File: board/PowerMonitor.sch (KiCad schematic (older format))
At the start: 0 parts

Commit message: Issue #934 - GTP routing
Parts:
- added C173, C174: C, ~, symbol C
- added U17: MAX4377, symbol MAX4377
- added U18: MAX4378, symbol MAX4378
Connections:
- new net DDR0V9_RS+: U18.10 (RS3+)
- new net DDR0V9_RS-: U18.9 (RS3-)
- new net DDR1V8_RS+: U18.12 (RS4+)
- new net DDR1V8_RS-: U18.13 (RS4-)
- new net GND: C173.2, C174.2, U17.4 (GND), U18.11 (GND)
- new net PICADC10: U18.8 (OUT3)
- new net PICADC11: U18.14 (OUT4)
- new net PICADC6: U17.1 (OUT1)
- new net PICADC7: U17.7 (OUT2)
- new net PICADC8: U18.1 (OUT1)
- new net PICADC9: U18.7 (OUT2)
- new net VCC12V0_RS+: U17.3 (RS1+)
- new net VCC12V0_RS-: U17.2 (RS1-)
- new net VCC1V2_RS+: U18.5 (RS2+)
- new net VCC1V2_RS-: U18.6 (RS2-)
- new net VCC3V3_RS+: U18.3 (RS1+)
- new net VCC3V3_RS-: U18.2 (RS1-)
- new net VCC5V0: C173.1, C174.1, U17.8 (VCC), U18.4 (VCC)
- new net VCC5V0_RS+: U17.5 (RS2+)
- new net VCC5V0_RS-: U17.6 (RS2-)
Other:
- note added: "CURRENT MONITORING"
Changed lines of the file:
@@
 $Descr A4 11693 8268
 encoding utf-8
-Sheet 7 8
+Sheet 8 8
 Title ""
-Date "25 feb 2014"
+Date "27 feb 2014"
 Rev ""
 Comp ""
@@
 Comment4 ""
 $EndDescr
+$Comp
+L MAX4377 U17
+U 1 1 530F8241
+P 1650 1350
+F 0 "U17" H 1950 1000 60  0000 C CNN
+F 1 "MAX4377" H 1550 1650 60  0000 C CNN
+F 2 "" H 1650 1350 60  0000 C CNN
+F 3 "" H 1650 1350 60  0000 C CNN
+	1    1650 1350
+	1    0    0    -1
+$EndComp
+$Comp
+L MAX4378 U18
+U 1 1 530F8250
+P 4250 1450
+F 0 "U18" H 4500 1000 60  0000 C CNN
+F 1 "MAX4378" H 4150 1900 60  0000 C CNN
+F 2 "" H 6150 100 60  0000 C CNN
+F 3 "" H 6150 100 60  0000 C CNN
+	1    4250 1450
+	1    0    0    -1
+$EndComp
+Text GLabel 2500 1200 2    39   Input ~ 0
+VCC5V0
+Wire Wire Line
+	2500 1200 2300 1200
+Text Label 2300 1200 0    39   ~ 0
+VCC5V0
+Text Label 3650 1450 2    39   ~ 0
+VCC5V0
+Text GLabel 850  1500 0    39   Input ~ 0
+GND
+Wire Wire Line
+	1050 1500 850  1500
+Text Label 850  1500 0    39   ~ 0
+GND
+Text Label 1050 1200 2    39   ~ 0
+PICADC6
+Text Label 2300 1300 0    39   ~ 0
+PICADC7
+Text Label 3650 1150 2    39   ~ 0
+PICADC8
+Text Label 3650 1750 2    39   ~ 0
+PICADC9
+Text Label 4850 1750 0    39   ~ 0
+PICADC10
+Text Label 4850 1150 0    39   ~ 0
+PICADC11
+Text HLabel 1050 1400 0    39   Input ~ 0
+VCC12V0_RS+
+Text HLabel 1050 1300 0    39   Input ~ 0
+VCC12V0_RS-
+Text HLabel 2300 1500 2    39   Input ~ 0
+VCC5V0_RS+
+Text HLabel 2300 1400 2    39   Input ~ 0
+VCC5V0_RS-
+Text HLabel 3650 1350 0    39   Input ~ 0
+VCC3V3_RS+
+Text HLabel 3650 1250 0    39   Input ~ 0
+VCC3V3_RS-
+Text HLabel 3650 1550 0    39   Input ~ 0
+VCC1V2_RS+
+Text HLabel 3650 1650 0    39   Input ~ 0
+VCC1V2_RS-
+Text HLabel 4850 1350 2    39   Input ~ 0
+DDR1V8_RS+
+Text HLabel 4850 1250 2    39   Input ~ 0
+DDR1V8_RS-
+Text HLabel 4850 1650 2    39   Input ~ 0
+DDR0V9_RS-
+Text HLabel 4850 1550 2    39   Input ~ 0
+DDR0V9_RS+
+$Comp
+L C C173
+U 1 1 5311983F
+P 1850 2550
+F 0 "C173" H 1850 2650 40  0000 L CNN
+F 1 "C" H 1856 2465 40  0000 L CNN
+F 2 "~" H 1888 2400 30  0000 C CNN
+F 3 "~" H 1850 2550 60  0000 C CNN
+	1    1850 2550
+	1    0    0    -1
+$EndComp
+Text Label 1650 2300 0    39   ~ 0
+VCC5V0
+Wire Wire Line
+	1650 2300 2100 2300
+Wire Wire Line
+	1850 2300 1850 2350
+$Comp
+L C C174
+U 1 1 53119855
+P 2100 2550
+F 0 "C174" H 2100 2650 40  0000 L CNN
+F 1 "C" H 2106 2465 40  0000 L CNN
+F 2 "~" H 2138 2400 30  0000 C CNN
+F 3 "~" H 2100 2550 60  0000 C CNN
+	1    2100 2550
+	1    0    0    -1
+$EndComp
+Wire Wire Line
+	2100 2300 2100 2350
+Connection ~ 1850 2300
+Wire Wire Line
+	1650 2750 2100 2750
+Connection ~ 1850 2750
+Text Label 4850 1450 0    39   ~ 0
+GND
+Text Label 1650 2750 0    39   ~ 0
+GND
+Wire Bus Line
+	6200 500  6200 3000
+Wire Bus Line
+	6200 3000 500  3000
+Text Notes 5450 2950 0    39   ~ 0
+CURRENT MONITORING
+Text HLabel 1250 3750 0    39   Input ~ 0
+PICADC0
+Text HLabel 1250 3850 0    39   Input ~ 0
+PICADC1
+Text HLabel 1250 3950 0    39   Input ~ 0
+PICADC2
+Text HLabel 1250 4050 0    39   Input ~ 0
+PICADC3
+Text HLabel 1250 4150 0    39   Input ~ 0
+PICADC4
+Text HLabel 1250 4250 0    39   Input ~ 0
+PICADC5
 $EndSCHEMATC

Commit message: Issue #1022 - Power supply & pic
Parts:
- added U?: PIC18F85J50, ~, symbol PIC18F85J50
- added X?: CRYSTAL, ~, symbol CRYSTAL
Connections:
- net VCC5V0 renamed VCC3V3
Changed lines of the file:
@@
 EELAYER 27 0
 EELAYER END
-$Descr A4 11693 8268
+$Descr A3 16535 11693
 encoding utf-8
 Sheet 8 8
 Title ""
-Date "13 mar 2014"
+Date "14 mar 2014"
 Rev ""
 Comp ""
@@
 $EndComp
 Text GLabel 2500 1200 2    39   Input ~ 0
-VCC5V0
+VCC3V3
 Wire Wire Line
 	2500 1200 2300 1200
@@
 Text HLabel 1250 4250 0    39   Input ~ 0
 PICADC5
+$Comp
+L CRYSTAL X?
+U 1 1 53234E61
+P 1400 6600
+F 0 "X?" H 1400 6750 60  0000 C CNN
+F 1 "CRYSTAL" H 1400 6450 60  0000 C CNN
+F 2 "~" H 1400 6600 60  0000 C CNN
+F 3 "~" H 1400 6600 60  0000 C CNN
+	1    1400 6600
+	1    0    0    -1
+$EndComp
+$Comp
+L PIC18F85J50 U?
+U 1 1 53239CEB
+P 8050 6600
+F 0 "U?" H 8900 7800 70  0000 C CNN
+F 1 "PIC18F85J50" H 8050 6600 60  0000 C CNN
+F 2 "~" H 8050 6600 60  0000 C CNN
+F 3 "~" H 8050 6600 60  0000 C CNN
+	1    8050 6600
+	1    0    0    -1
+$EndComp
 $EndSCHEMATC

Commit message: Issue #1022 - Power supply & pic& SCHEMATIC SECTION.
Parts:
- added C175, C178, C179, C180, C181, C182, C183: 0.1mfd, ~, symbol C
- added C176, C177: 22pf, ~, symbol C
- added D10, D11, D12, D13, D14, D15, D16, D17, D18, D19, D20, D21, D22, D23, D24, D25, D26, D27, D3, D4, D5, D6, D7, D8, D9: LED, ~, symbol LED
- added J10: USB_MICRO_B, ~, symbol USB_MICRO_B
- added P48: CONN_6, symbol CONN_6
- added R147: 10K, ~, symbol R
- added R149, R151, R153, R159, R287, R288: 1K, ~, symbol RES_NET4
- added R307: 1.5K, ~, symbol R
- added VR1, VR2: VR, ~, symbol VR
- C173, C174: value C -> 0.1mfd
- gave numbers to parts that had none: 2
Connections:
- net labels added: LED1, LED10, LED11, LED12, LED13, LED14, LED15, LED16, LED17, LED18, LED19, LED2, LED20, LED21, LED22, LED23, LED24, LED25, LED3, LED4, LED5, LED6, LED7, LED8, LED9, MCLR, OSC1, OSC2, PGC, PGD, RE232RX, RS232TX, RS422RX, RS422TX, SCK, SPI-CS_FLASH, SPI-SDI, SPI-SDO, TCK, TDO-USB/TDI-FPGA, TDO_FPGA/TDO-JTAG, TMS, USB_DM, USB_DP
- wire segments 6 -> 170
- no-connect marks 0 -> 3
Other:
- moved on the sheet: U19, X2

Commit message: Issue #1022 - Cypress
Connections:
- wire segments 170 -> 169
- no-connect marks 3 -> 15
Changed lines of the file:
@@
 Text Label 1000 8500 0    39   ~ 0
 VCC3V3
-Text Label 1850 8500 2    39   ~ 0
+Wire Wire Line
+	1700 8500 1850 8500
+Wire Wire Line
+	1200 8500 1000 8500
+Text Label 3300 6750 2    39   ~ 0
 MCLR
-Wire Wire Line
-	1700 8500 1850 8500
-Wire Wire Line
-	1200 8500 1000 8500
-Text Label 3050 6750 0    39   ~ 0
-MCLR
-Wire Wire Line
-	3050 6750 3300 6750
 Wire Wire Line
 	3300 6600 3050 6600
@@
 Text HLabel 6650 4850 1    39   Input ~ 0
 TDO_FPGA/TDO-JTAG
+NoConn ~ 4550 4850
+NoConn ~ 4700 4850
+NoConn ~ 4850 4850
+NoConn ~ 5000 4850
+NoConn ~ 5150 4850
+NoConn ~ 5300 4850
+NoConn ~ 5450 4850
+NoConn ~ 5600 4850
+NoConn ~ 5750 4850
+NoConn ~ 7100 4850
+NoConn ~ 3050 6900
+NoConn ~ 3050 6600
+Text Label 1850 8500 2    39   ~ 0
+MCLR
 $EndSCHEMATC

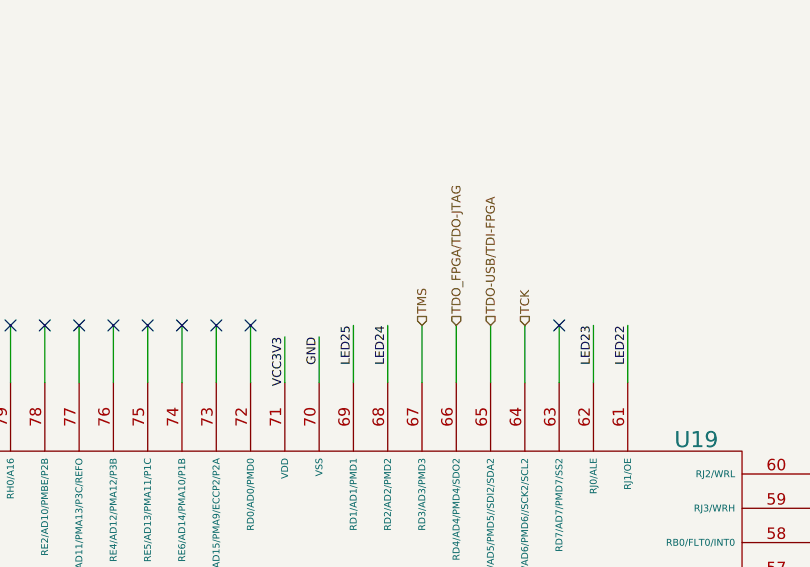
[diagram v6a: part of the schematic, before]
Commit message: Issue #1022 - Reset signals
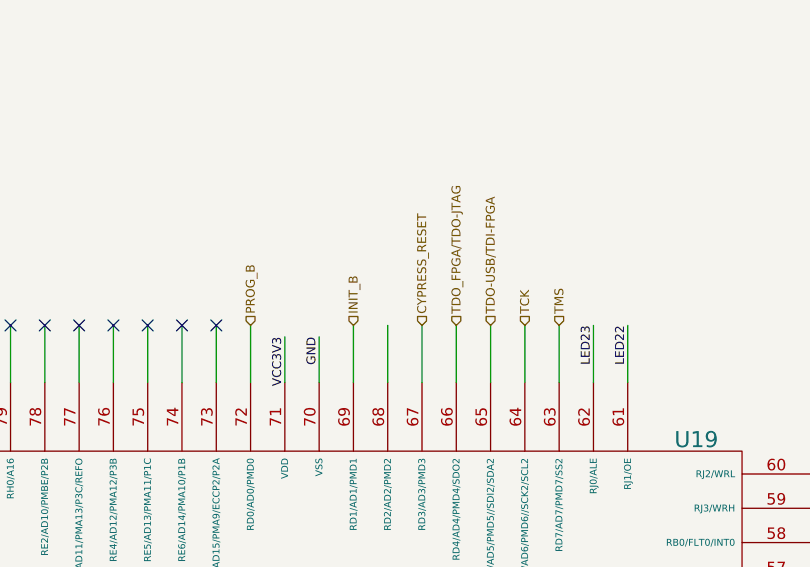
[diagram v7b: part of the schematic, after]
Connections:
- net LED24: no longer U19.68 (RD2/AD2/PMD2)
- net LED25: no longer U19.69 (RD1/AD1/PMD1)
- net TMS: now also U19.63 (RD7/AD7/PMD7/SS2); no longer U19.67 (RD3/AD3/PMD3)
- net PROG_B: now reaches U19.72 (RD0/AD0/PMD0)
- new net CYPRESS_RESET: U19.67 (RD3/AD3/PMD3)
- new net INIT_B: U19.69 (RD1/AD1/PMD1)
- no-connect marks 15 -> 13
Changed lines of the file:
@@
 Sheet 7 8
 Title ""
-Date "18 mar 2014"
+Date "25 mar 2014"
 Rev ""
 Comp ""
@@
 Text Label 7250 4850 3    39   ~ 0
 LED23
-Text Label 6350 4850 3    39   ~ 0
-LED24
-Text Label 6200 4850 3    39   ~ 0
-LED25
 Wire Wire Line
 	3300 6900 3050 6900
@@
 Text Label 12400 9450 0    39   ~ 0
 GND
-Text HLabel 6500 4850 1    39   Input ~ 0
+Text HLabel 7100 4850 1    39   Input ~ 0
 TMS
 Text HLabel 6950 4850 1    39   Input ~ 0
@@
 NoConn ~ 5450 4850
 NoConn ~ 5600 4850
-NoConn ~ 5750 4850
-NoConn ~ 7100 4850
 NoConn ~ 3050 6900
 NoConn ~ 3050 6600
 Text Label 1850 8500 2    39   ~ 0
 MCLR
+Text HLabel 5750 4850 1    39   Input ~ 0
+PROG_B
+Text HLabel 6200 4850 1    39   Input ~ 0
+INIT_B
+Text HLabel 6500 4850 1    39   Input ~ 0
+CYPRESS_RESET
 $EndSCHEMATC

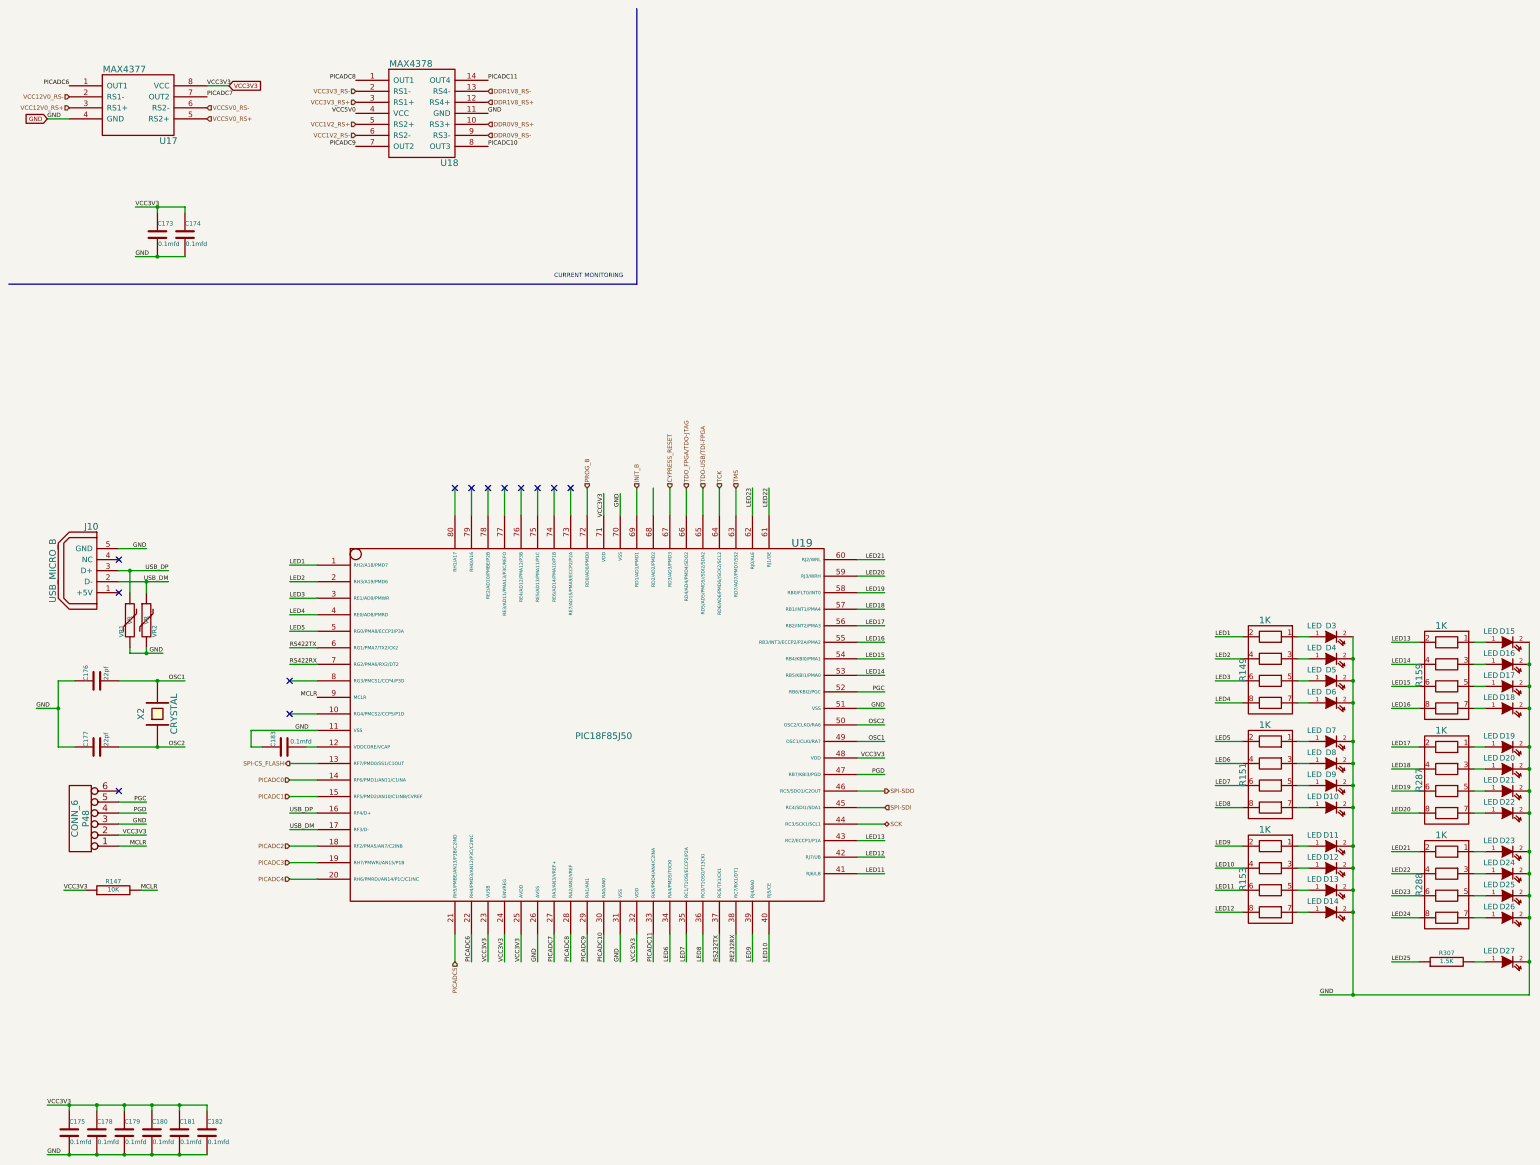
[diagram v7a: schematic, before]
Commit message: Issue #1022 - Reset signals
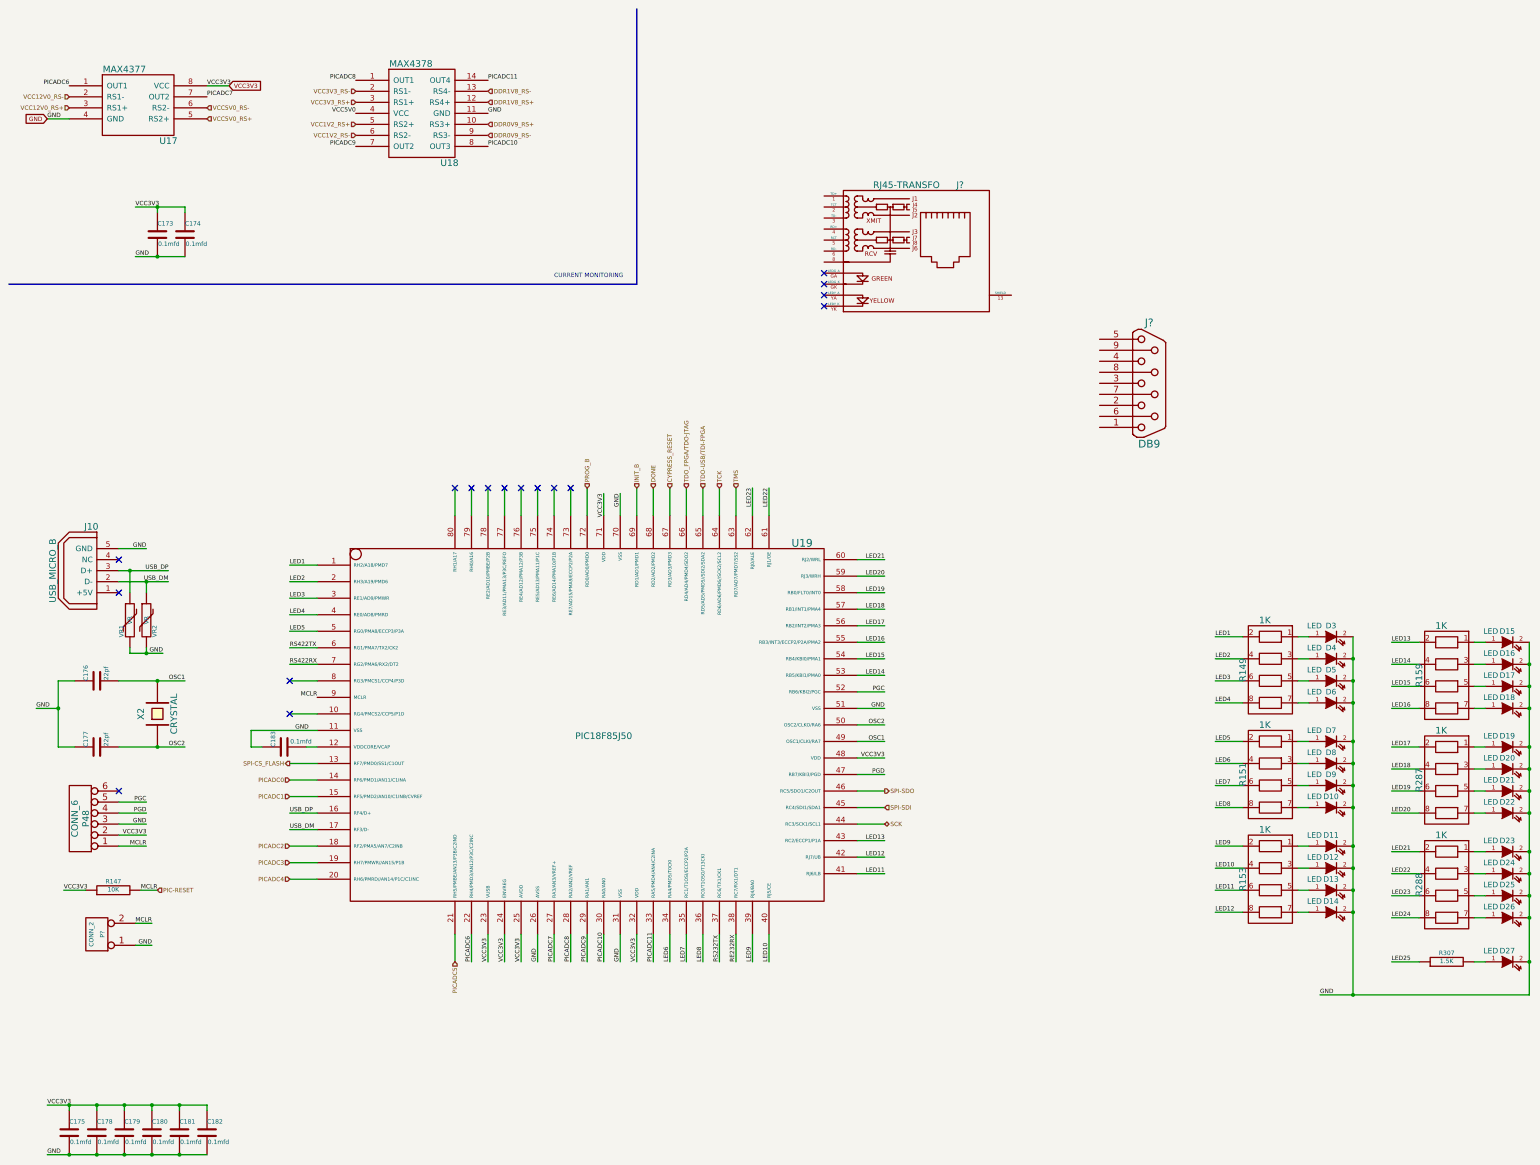
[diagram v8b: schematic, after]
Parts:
- added J?: DB9, symbol DB9
- added J?: RJ45-TRANSFO, symbol RJ45-TRANSFO
- added P?: CONN_2, symbol CONN_2
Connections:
- net GND: now also P?.1 (P1)
- net DONE: now reaches U19.68 (RD2/AD2/PMD2)
- net MCLR renamed PIC-RESET
- net PIC-RESET: now also P?.2 (PM)
- no-connect marks 13 -> 17
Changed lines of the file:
@@
 Sheet 7 8
 Title ""
-Date "25 mar 2014"
+Date "26 mar 2014"
 Rev ""
 Comp ""
@@
 Text HLabel 6500 4850 1    39   Input ~ 0
 CYPRESS_RESET
+Text HLabel 6350 4850 1    39   Input ~ 0
+DONE
+$Comp
+L CONN_2 P?
+U 1 1 5333ADD5
+P 1300 8900
+F 0 "P?" V 1250 8900 40  0000 C CNN
+F 1 "CONN_2" V 1350 8900 40  0000 C CNN
+F 2 "" H 1300 8900 60  0000 C CNN
+F 3 "" H 1300 8900 60  0000 C CNN
+	1    1300 8900
+	-1   0    0    1
+$EndComp
+Text Label 1800 8800 2    39   ~ 0
+MCLR
+Wire Wire Line
+	1650 8800 1800 8800
+Text Label 1800 9000 2    39   ~ 0
+GND
+Wire Wire Line
+	1650 9000 1800 9000
+Text HLabel 1850 8500 2    39   Input ~ 0
+PIC-RESET
+$Comp
+L DB9 J?
+U 1 1 53370367
+P 10850 3900
+F 0 "J?" H 10850 4450 70  0000 C CNN
+F 1 "DB9" H 10850 3350 70  0000 C CNN
+F 2 "" H 10850 3900 60  0000 C CNN
+F 3 "" H 10850 3900 60  0000 C CNN
+	1    10850 3900
+	1    0    0    -1
+$EndComp
+$Comp
+L RJ45-TRANSFO J?
+U 1 1 53370E0F
+P 9000 2700
+F 0 "J?" H 9100 3300 60  0000 L CNN
+F 1 "RJ45-TRANSFO" H 8950 3300 60  0000 R CNN
+F 2 "" H 9000 2700 60  0000 C CNN
+F 3 "" H 9000 2700 60  0000 C CNN
+	1    9000 2700
+	1    0    0    -1
+$EndComp
+NoConn ~ 7900 2900
+NoConn ~ 7900 3000
+NoConn ~ 7900 3100
+NoConn ~ 7900 3200
 $EndSCHEMATC
